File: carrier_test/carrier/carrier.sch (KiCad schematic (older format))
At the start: 2 parts

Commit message: updated schematic
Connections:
- net labels added: PA0_KEY_UP, PA10_USART1_RX, PA11_USB_OTG_FS_DM, PA12_USB_OTG_FS_DP, PA1_ENC3_B, PA2_ADC_TEMP, PA3_ADC1_IN3, PA5_TIM_ENC3_A, PA6_O_LED1, PA7_O_LED2, PA9_USART1_TX, PB0_O_FLASH_CS, PB10_USART3_TX, PB11_USART3_RX, PB12_I_MOT_FAULT1, PB13_I_MOT_FAULT2, PB1_O_SPI_CS2, PB3_SPI1_SCK, PB5_SPI1_MOSI, PB6_I2C1_SCL, PB7_I2C1_SDA, PB8_O_PWR_EN, PC0_ADC_MOT1_CUR, PC10_SDIO_D2, PC11_SDIO_D3, PC12_SDIO_CK, PC1_ADC_MOT2_CUR, PC2_ADC_MOT3_CUR, PC3_ADC1_IN13, PC4_ADC_BATT_CUR, PC5_ADC_BATT_VOL, PC6_TIM_ENC1_A, PC7_TIM_ENC1_B, PC8_SDIO_D0, PC9_SDIO_D1, PD12_TIM_ENC2_A, PD13_TIM_ENC2_B, PD2__SDIO_CMD, PD5_USART2_TX, PD6_USART2_RX, PE0_O_PWR_MOT_EN, PE10_TIM_MOT2_B, PE11_TIM_MOT2_A, PE12_TIM_MOT3_A, PE13_TIM_MOT3_A, PE14_O_MOT_ENABLE, PE15_TIM1_BKIN, PE1_O_PWR_SBC_EN, PE3_KEY1, PE4_KEY0, PE5_TIM_FAN_PWM, PE6_I_FAN_INDEX, PE7_O_SPI_CS3, PE8_TIM_MOT1_B, PE9_TIM_MOT1_A, V_MOT
- net labels removed: PA0, PA1, PA10, PA11, PA12, PA2, PA3, PA5, PA6, PA7, PA9, PB0, PB1, PB10, PB11, PB12, PB13, PB3, PB5, PB6, PB7, PB8, PC0, PC1, PC10, PC11, PC12, PC2, PC3, PC4, PC5, PC6, PC7, PC8, PC9, PD12, PD13, PD2, PD5, PD6, PE0, PE1, PE10, PE11, PE12, PE13, PE14, PE15, PE3, PE4, PE5, PE6, PE7, PE8, PE9, VREF+, VREF-
- wire segments 117 -> 121
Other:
- note added: "PB4/SPI1_MISO is \nmissing from header!!!"

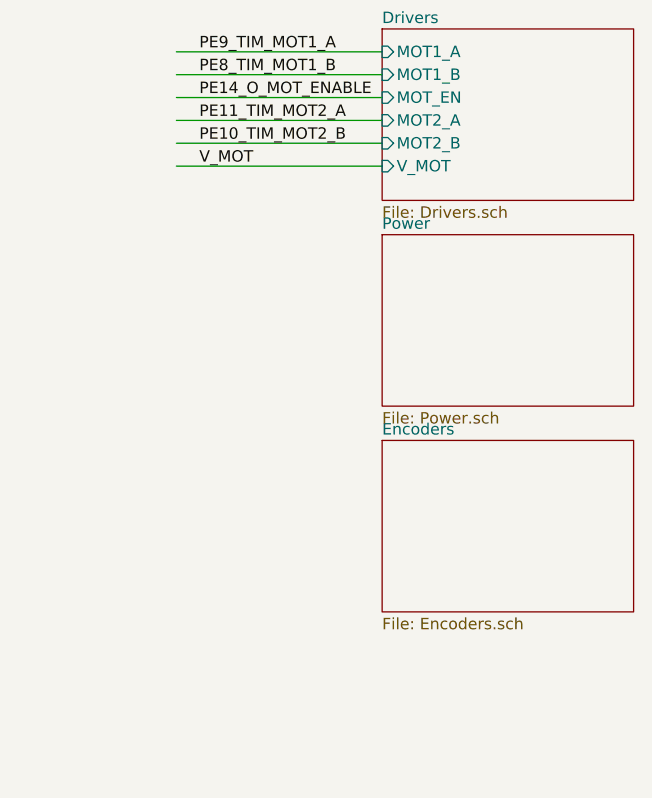
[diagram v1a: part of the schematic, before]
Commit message: update schematic
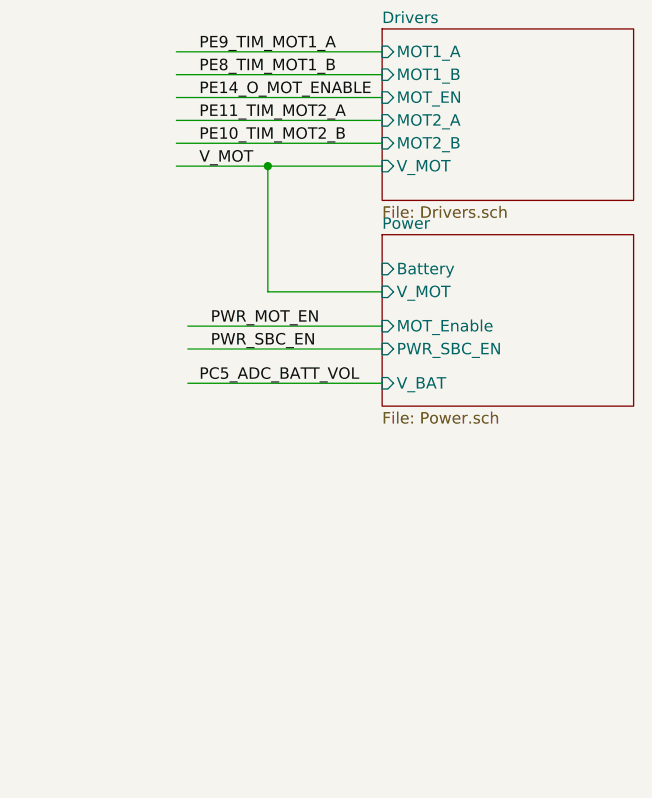
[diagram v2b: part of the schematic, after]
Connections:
- net labels added: PWR_MOT_EN, PWR_SBC_EN
- wire segments 121 -> 127
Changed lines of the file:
@@
 $Descr A4 11693 8268
 encoding utf-8
-Sheet 1 4
+Sheet 1 3
 Title ""
 Date ""
@@
 F0 "Power" 50
 F1 "Power.sch" 50
-$EndSheet
-$Sheet
-S 9600 2650 1100 750
-U 5B513203
-F0 "Encoders" 50
-F1 "Encoders.sch" 50
+F2 "Battery" I L 9600 1900 50
+F3 "MOT_Enable" I L 9600 2150 50
+F4 "V_MOT" I L 9600 2000 50
+F5 "PWR_SBC_EN" I L 9600 2250 50
+F6 "V_BAT" I L 9600 2400 50
 $EndSheet
 Text Label 8800 950  0    50   ~ 0
@@
 	8700 1350 9600 1350
 Wire Wire Line
-	8700 1450 9600 1450
+	8700 1450 9100 1450
+Wire Wire Line
+	9600 2000 9100 2000
+Wire Wire Line
+	9100 2000 9100 1450
+Connection ~ 9100 1450
+Wire Wire Line
+	9100 1450 9600 1450
+Text Label 8850 2150 0    50   ~ 0
+PWR_MOT_EN
+Text Label 8850 2250 0    50   ~ 0
+PWR_SBC_EN
+Wire Wire Line
+	8750 2150 9600 2150
+Wire Wire Line
+	8750 2250 9600 2250
+Text Label 8800 2400 0    50   ~ 0
+PC5_ADC_BATT_VOL
+Wire Wire Line
+	8750 2400 9600 2400
 $EndSCHEMATC

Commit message: Fix supply, add gps/imu serial, oled
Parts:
- added C1, C2, C3, C4, C5, C6: C, symbol agg-kicad:C
- added D1: SCHOTTKY, symbol agg-kicad:SCHOTTKY
- added J3: IMU, symbol agg-kicad:CONN_01x04
- added J4: GPS, symbol agg-kicad:CONN_01x04
- added J5: OLED, symbol agg-kicad:CONN_01x04
- gave numbers to parts that had none: 2
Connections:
- net labels added: PB2_I_BT1
- net labels removed: BT1, PB2, PWR_MOT_EN, PWR_SBC_EN
- wire segments 127 -> 168

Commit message: Schematic update
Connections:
- wire segments 168 -> 170
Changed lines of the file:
@@
 F6 "V_BAT" I L 7200 4550 50
 F7 "I_BAT" I L 7200 4700 50
+F8 "Temp" I L 7200 4850 50
+F9 "FAN_ON" I L 7200 4950 50
+F10 "AUX_ON" I L 7200 5050 50
 $EndSheet
 Text Label 6350 1650 0    50   ~ 0
@@
 Wire Wire Line
 	4400 6200 5300 6200
+Text Label 6400 4850 0    50   ~ 0
+PA2_ADC_TEMP
+Wire Wire Line
+	6350 4850 7200 4850
+Text Label 6400 4950 0    50   ~ 0
+PE5_TIM_FAN_PWM
+Wire Wire Line
+	6350 4950 7200 4950
 $EndSCHEMATC

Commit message: Updates
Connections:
- net labels added: PB15_TIM_AUX2_PWM, PB9_TIM_AUX_PWM, PC13_I_FAN_INDEX, PE6_TIM_AUX3_PWM
- net labels removed: PB15, PB9, PC13, PE6_I_FAN_INDEX
- wire segments 170 -> 172
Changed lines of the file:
@@
 PE4_KEY0
 Text Label 1250 2200 0    50   ~ 0
-PE6_I_FAN_INDEX
+PE6_TIM_AUX3_PWM
 Text Label 1250 2300 0    50   ~ 0
 PC0_ADC_MOT1_CUR
@@
 Text Label 2600 3500 0    50   ~ 0
 PE14_O_MOT_ENABLE
-Text Label 2850 2200 0    50   ~ 0
-PC13
+Text Label 2600 2200 0    50   ~ 0
+PC13_I_FAN_INDEX
 Text Label 2600 3600 0    50   ~ 0
 PB10_USART3_TX
@@
 PE1_O_PWR_SBC_EN
 Text Label 1300 5000 0    50   ~ 0
-PB9
+PB9_TIM_AUX_PWM
 Text Label 1300 5200 0    50   ~ 0
 PB5_SPI1_MOSI
@@
 PD9
 Text Label 2600 6700 0    50   ~ 0
-PB15
+PB15_TIM_AUX2_PWM
 Wire Wire Line
 	2550 1900 3250 1900
@@
 F9 "FAN_ON" I L 7200 4950 50
 F10 "AUX_ON" I L 7200 5050 50
+F11 "FAN_INDEX" I L 7200 5150 50
 $EndSheet
 Text Label 6350 1650 0    50   ~ 0
@@
 Wire Wire Line
 	6350 4950 7200 4950
+Text Label 6400 5050 0    50   ~ 0
+PE6_TIM_AUX3_PWM
+Wire Wire Line
+	6350 5050 7200 5050
+Text Label 6400 5150 0    50   ~ 0
+PC13_I_FAN_INDEX
+Wire Wire Line
+	6350 5150 7200 5150
 $EndSCHEMATC
